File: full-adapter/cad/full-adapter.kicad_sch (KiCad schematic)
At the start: 0 parts

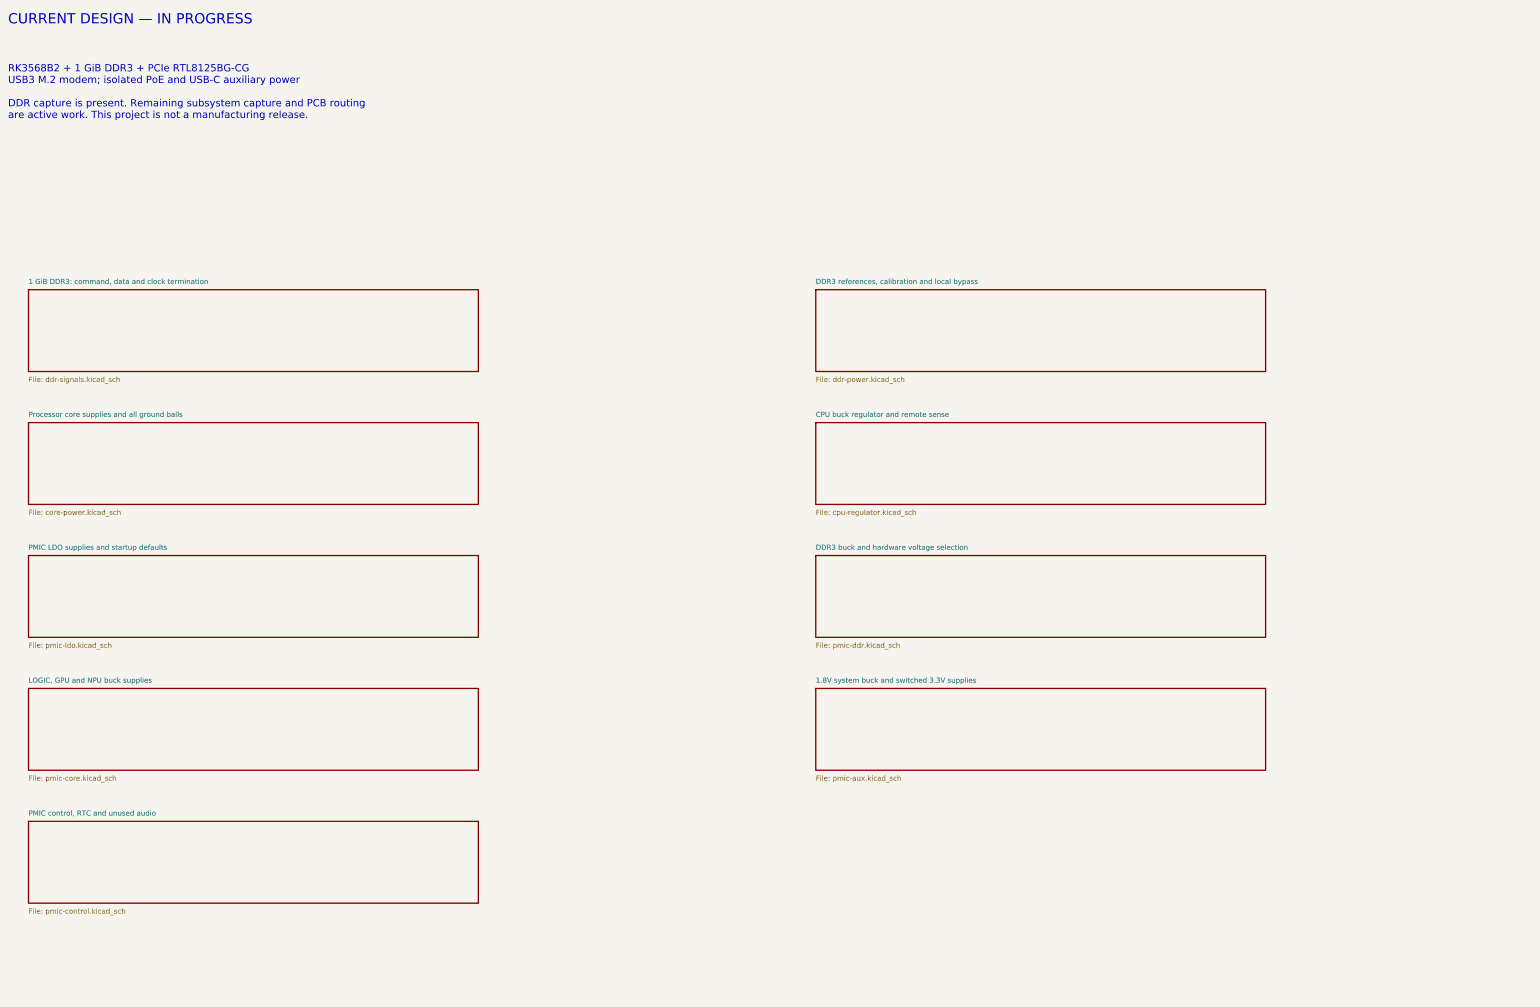
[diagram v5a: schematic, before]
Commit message: Capture processor analog and IO supplies with USB filtering
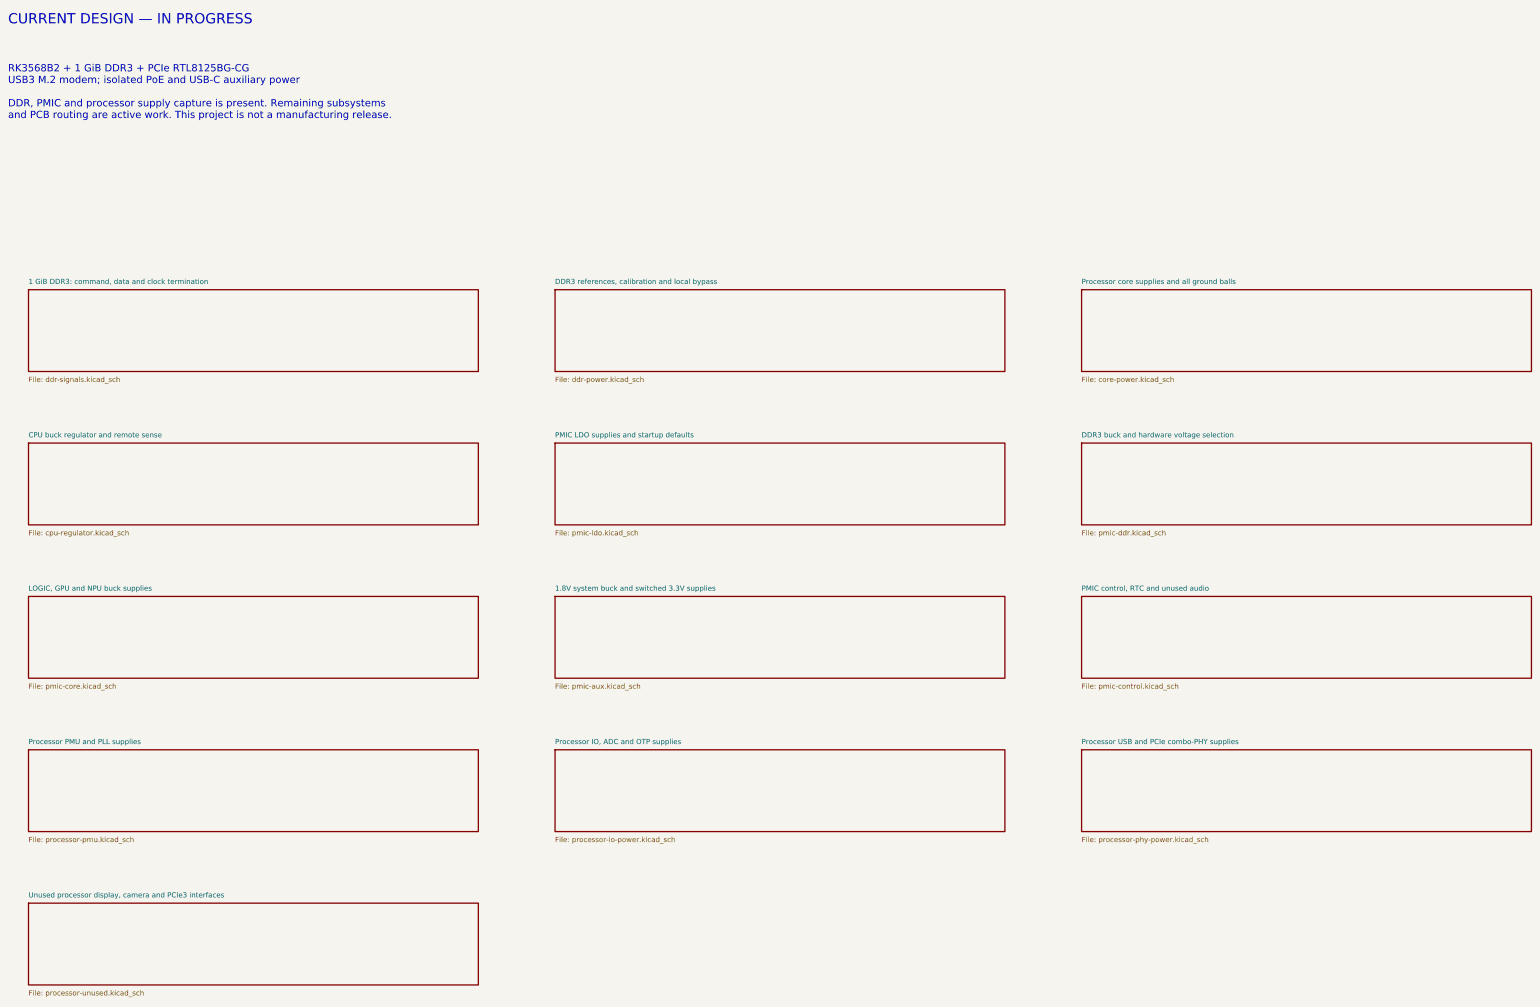
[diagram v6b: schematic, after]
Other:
- added sheet Processor IO, ADC and OTP supplies (processor-io-power.kicad_sch)
- added sheet Processor PMU and PLL supplies (processor-pmu.kicad_sch)
- added sheet Processor USB and PCIe combo-PHY supplies (processor-phy-power.kicad_sch)
- added sheet Unused processor display, camera and PCIe3 interfaces (processor-unused.kicad_sch)
- note added: "RK3568B2 + 1 GiB DDR3 + PCIe RTL8125BG-CG USB3 M.2 modem; isolated PoE and USB-C auxiliary power DDR, PMIC and processor supply capture is present. Remaining subsystems and PCB routing are active work. This project is not a manufacturing release."
- note removed: "RK3568B2 + 1 GiB DDR3 + PCIe RTL8125BG-CG USB3 M.2 modem; isolated PoE and USB-C auxiliary power DDR capture is present. Remaining subsystem capture and PCB routing are active work. This project is not a manufacturing release."
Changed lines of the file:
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@@
 (title_block (title "Integrated Linux USB3 modem / 2.5GbE development board") (rev "WORK IN PROGRESS") (company "Integrated modem development board"))
 (text "CURRENT DESIGN — IN PROGRESS" (at 20.32 20.32 0) (effects (font (size 2.54 2.54)) (justify left top)))
-(text "RK3568B2 + 1 GiB DDR3 + PCIe RTL8125BG-CG\nUSB3 M.2 modem; isolated PoE and USB-C auxiliary power\n\nDDR capture is present. Remaining subsystem capture and PCB routing\nare active work. This project is not a manufacturing release." (at 20.32 33.02 0) (effects (font (size 1.8 1.8)) (justify left top)))
+(text "RK3568B2 + 1 GiB DDR3 + PCIe RTL8125BG-CG\nUSB3 M.2 modem; isolated PoE and USB-C auxiliary power\n\nDDR, PMIC and processor supply capture is present. Remaining subsystems\nand PCB routing are active work. This project is not a manufacturing release." (at 20.32 33.02 0) (effects (font (size 1.8 1.8)) (justify left top)))
 (sheet (at 25.4 88.9) (size 111.76 20.32) (fields_autoplaced yes) (stroke (width 0.254) (type default)) (fill (color 0 0 0 0)) (property "Sheetname" "1 GiB DDR3: command, data and clock termination" (at 25.4 87.63000000000001 0) (effects (font (size 1.27 1.27)) (justify left bottom))) (property "Sheetfile" "ddr-signals.kicad_sch" (at 25.4 110.49000000000001 0) (effects (font (size 1.27 1.27)) (justify left top))))
-(sheet (at 220.98000000000002 88.9) (size 111.76 20.32) (fields_autoplaced yes) (stroke (width 0.254) (type default)) (fill (color 0 0 0 0)) (property "Sheetname" "DDR3 references, calibration and local bypass" (at 220.98000000000002 87.63000000000001 0) (effects (font (size 1.27 1.27)) (justify left bottom))) (property "Sheetfile" "ddr-power.kicad_sch" (at 220.98000000000002 110.49000000000001 0) (effects (font (size 1.27 1.27)) (justify left top))))
-(sheet (at 25.4 121.92000000000002) (size 111.76 20.32) (fields_autoplaced yes) (stroke (width 0.254) (type default)) (fill (color 0 0 0 0)) (property "Sheetname" "Processor core supplies and all ground balls" (at 25.4 120.65000000000002 0) (effects (font (size 1.27 1.27)) (justify left bottom))) (property "Sheetfile" "core-power.kicad_sch" (at 25.4 143.51000000000002 0) (effects (font (size 1.27 1.27)) (justify left top))))
-(sheet (at 220.98000000000002 121.92000000000002) (size 111.76 20.32) (fields_autoplaced yes) (stroke (width 0.254) (type default)) (fill (color 0 0 0 0)) (property "Sheetname" "CPU buck regulator and remote sense" (at 220.98000000000002 120.65000000000002 0) (effects (font (size 1.27 1.27)) (justify left bottom))) (property "Sheetfile" "cpu-regulator.kicad_sch" (at 220.98000000000002 143.51000000000002 0) (effects (font (size 1.27 1.27)) (justify left top))))
-(sheet (at 25.4 154.94) (size 111.76 20.32) (fields_autoplaced yes) (stroke (width 0.254) (type default)) (fill (color 0 0 0 0)) (property "Sheetname" "PMIC LDO supplies and startup defaults" (at 25.4 153.67 0) (effects (font (size 1.27 1.27)) (justify left bottom))) (property "Sheetfile" "pmic-ldo.kicad_sch" (at 25.4 176.53 0) (effects (font (size 1.27 1.27)) (justify left top))))
-(sheet (at 220.98000000000002 154.94) (size 111.76 20.32) (fields_autoplaced yes) (stroke (width 0.254) (type default)) (fill (color 0 0 0 0)) (property "Sheetname" "DDR3 buck and hardware voltage selection" (at 220.98000000000002 153.67 0) (effects (font (size 1.27 1.27)) (justify left bottom))) (property "Sheetfile" "pmic-ddr.kicad_sch" (at 220.98000000000002 176.53 0) (effects (font (size 1.27 1.27)) (justify left top))))
-(sheet (at 25.4 187.96) (size 111.76 20.32) (fields_autoplaced yes) (stroke (width 0.254) (type default)) (fill (color 0 0 0 0)) (property "Sheetname" "LOGIC, GPU and NPU buck supplies" (at 25.4 186.69 0) (effects (font (size 1.27 1.27)) (justify left bottom))) (property "Sheetfile" "pmic-core.kicad_sch" (at 25.4 209.55 0) (effects (font (size 1.27 1.27)) (justify left top))))
-(sheet (at 220.98000000000002 187.96) (size 111.76 20.32) (fields_autoplaced yes) (stroke (width 0.254) (type default)) (fill (color 0 0 0 0)) (property "Sheetname" "1.8V system buck and switched 3.3V supplies" (at 220.98000000000002 186.69 0) (effects (font (size 1.27 1.27)) (justify left bottom))) (property "Sheetfile" "pmic-aux.kicad_sch" (at 220.98000000000002 209.55 0) (effects (font (size 1.27 1.27)) (justify left top))))
-(sheet (at 25.4 220.98000000000002) (size 111.76 20.32) (fields_autoplaced yes) (stroke (width 0.254) (type default)) (fill (color 0 0 0 0)) (property "Sheetname" "PMIC control, RTC and unused audio" (at 25.4 219.71 0) (effects (font (size 1.27 1.27)) (justify left bottom))) (property "Sheetfile" "pmic-control.kicad_sch" (at 25.4 242.57000000000002 0) (effects (font (size 1.27 1.27)) (justify left top))))
+(sheet (at 156.21 88.9) (size 111.76 20.32) (fields_autoplaced yes) (stroke (width 0.254) (type default)) (fill (color 0 0 0 0)) (property "Sheetname" "DDR3 references, calibration and local bypass" (at 156.21 87.63000000000001 0) (effects (font (size 1.27 1.27)) (justify left bottom))) (property "Sheetfile" "ddr-power.kicad_sch" (at 156.21 110.49000000000001 0) (effects (font (size 1.27 1.27)) (justify left top))))
+(sheet (at 287.02 88.9) (size 111.76 20.32) (fields_autoplaced yes) (stroke (width 0.254) (type default)) (fill (color 0 0 0 0)) (property "Sheetname" "Processor core supplies and all ground balls" (at 287.02 87.63000000000001 0) (effects (font (size 1.27 1.27)) (justify left bottom))) (property "Sheetfile" "core-power.kicad_sch" (at 287.02 110.49000000000001 0) (effects (font (size 1.27 1.27)) (justify left top))))
+(sheet (at 25.4 127.0) (size 111.76 20.32) (fields_autoplaced yes) (stroke (width 0.254) (type default)) (fill (color 0 0 0 0)) (property "Sheetname" "CPU buck regulator and remote sense" (at 25.4 125.73 0) (effects (font (size 1.27 1.27)) (justify left bottom))) (property "Sheetfile" "cpu-regulator.kicad_sch" (at 25.4 148.59 0) (effects (font (size 1.27 1.27)) (justify left top))))
+(sheet (at 156.21 127.0) (size 111.76 20.32) (fields_autoplaced yes) (stroke (width 0.254) (type default)) (fill (color 0 0 0 0)) (property "Sheetname" "PMIC LDO supplies and startup defaults" (at 156.21 125.73 0) (effects (font (size 1.27 1.27)) (justify left bottom))) (property "Sheetfile" "pmic-ldo.kicad_sch" (at 156.21 148.59 0) (effects (font (size 1.27 1.27)) (justify left top))))
+(sheet (at 287.02 127.0) (size 111.76 20.32) (fields_autoplaced yes) (stroke (width 0.254) (type default)) (fill (color 0 0 0 0)) (property "Sheetname" "DDR3 buck and hardware voltage selection" (at 287.02 125.73 0) (effects (font (size 1.27 1.27)) (justify left bottom))) (property "Sheetfile" "pmic-ddr.kicad_sch" (at 287.02 148.59 0) (effects (font (size 1.27 1.27)) (justify left top))))
+(sheet (at 25.4 165.10000000000002) (size 111.76 20.32) (fields_autoplaced yes) (stroke (width 0.254) (type default)) (fill (color 0 0 0 0)) (property "Sheetname" "LOGIC, GPU and NPU buck supplies" (at 25.4 163.83 0) (effects (font (size 1.27 1.27)) (justify left bottom))) (property "Sheetfile" "pmic-core.kicad_sch" (at 25.4 186.69000000000003 0) (effects (font (size 1.27 1.27)) (justify left top))))
+(sheet (at 156.21 165.10000000000002) (size 111.76 20.32) (fields_autoplaced yes) (stroke (width 0.254) (type default)) (fill (color 0 0 0 0)) (property "Sheetname" "1.8V system buck and switched 3.3V supplies" (at 156.21 163.83 0) (effects (font (size 1.27 1.27)) (justify left bottom))) (property "Sheetfile" "pmic-aux.kicad_sch" (at 156.21 186.69000000000003 0) (effects (font (size 1.27 1.27)) (justify left top))))
+(sheet (at 287.02 165.10000000000002) (size 111.76 20.32) (fields_autoplaced yes) (stroke (width 0.254) (type default)) (fill (color 0 0 0 0)) (property "Sheetname" "PMIC control, RTC and unused audio" (at 287.02 163.83 0) (effects (font (size 1.27 1.27)) (justify left bottom))) (property "Sheetfile" "pmic-control.kicad_sch" (at 287.02 186.69000000000003 0) (effects (font (size 1.27 1.27)) (justify left top))))
+(sheet (at 25.4 203.20000000000002) (size 111.76 20.32) (fields_autoplaced yes) (stroke (width 0.254) (type default)) (fill (color 0 0 0 0)) (property "Sheetname" "Processor PMU and PLL supplies" (at 25.4 201.93 0) (effects (font (size 1.27 1.27)) (justify left bottom))) (property "Sheetfile" "processor-pmu.kicad_sch" (at 25.4 224.79000000000002 0) (effects (font (size 1.27 1.27)) (justify left top))))
+(sheet (at 156.21 203.20000000000002) (size 111.76 20.32) (fields_autoplaced yes) (stroke (width 0.254) (type default)) (fill (color 0 0 0 0)) (property "Sheetname" "Processor IO, ADC and OTP supplies" (at 156.21 201.93 0) (effects (font (size 1.27 1.27)) (justify left bottom))) (property "Sheetfile" "processor-io-power.kicad_sch" (at 156.21 224.79000000000002 0) (effects (font (size 1.27 1.27)) (justify left top))))
+(sheet (at 287.02 203.20000000000002) (size 111.76 20.32) (fields_autoplaced yes) (stroke (width 0.254) (type default)) (fill (color 0 0 0 0)) (property "Sheetname" "Processor USB and PCIe combo-PHY supplies" (at 287.02 201.93 0) (effects (font (size 1.27 1.27)) (justify left bottom))) (property "Sheetfile" "processor-phy-power.kicad_sch" (at 287.02 224.79000000000002 0) (effects (font (size 1.27 1.27)) (justify left top))))
+(sheet (at 25.4 241.3) (size 111.76 20.32) (fields_autoplaced yes) (stroke (width 0.254) (type default)) (fill (color 0 0 0 0)) (property "Sheetname" "Unused processor display, camera and PCIe3 interfaces" (at 25.4 240.03 0) (effects (font (size 1.27 1.27)) (justify left bottom))) (property "Sheetfile" "processor-unused.kicad_sch" (at 25.4 262.89 0) (effects (font (size 1.27 1.27)) (justify left top))))
 )

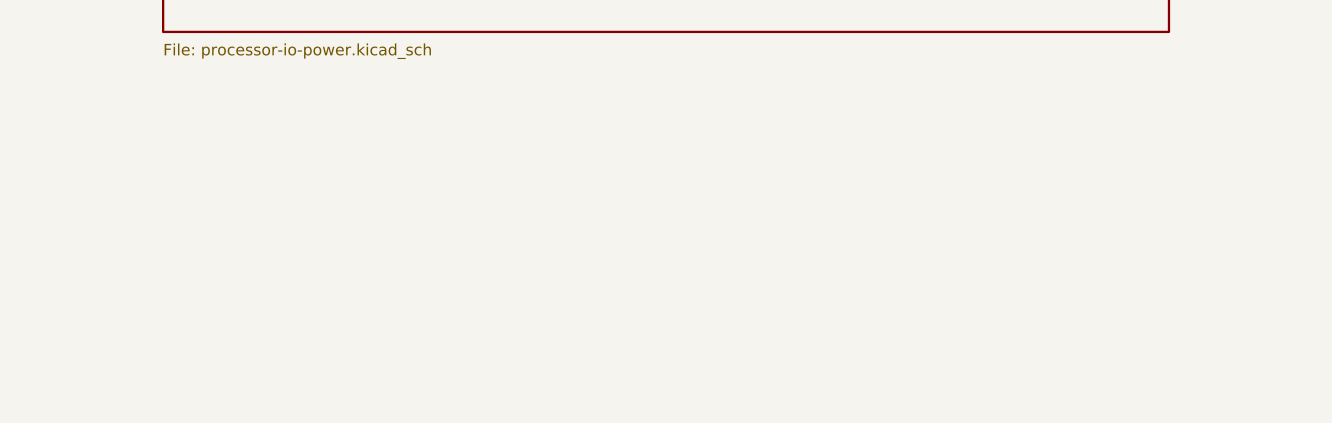
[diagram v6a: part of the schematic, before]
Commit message: Connect processor PMIC controls and hardware boot straps
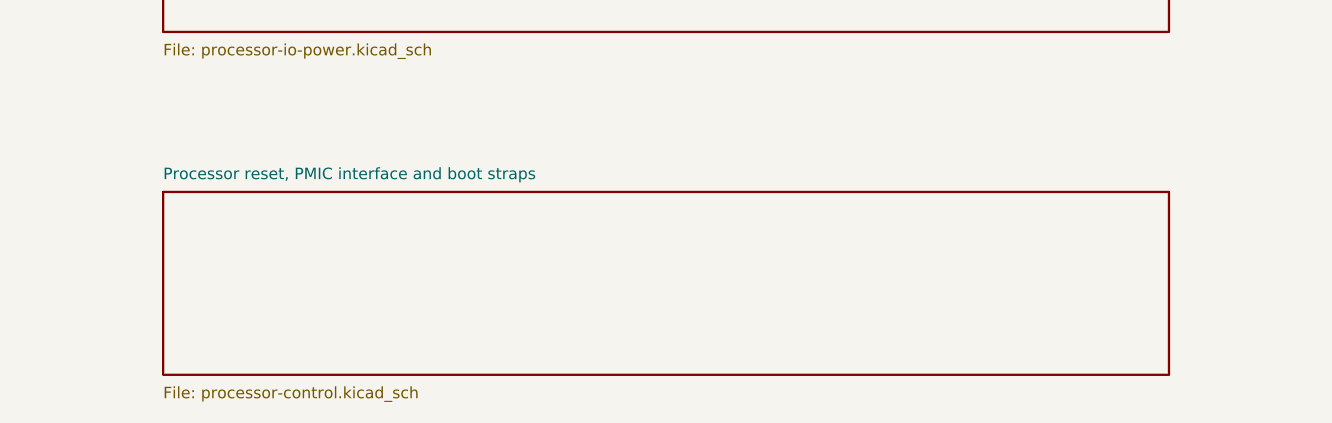
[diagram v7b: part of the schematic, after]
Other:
- added sheet Processor reset, PMIC interface and boot straps (processor-control.kicad_sch)
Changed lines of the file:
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@@
 (sheet (at 287.02 203.20000000000002) (size 111.76 20.32) (fields_autoplaced yes) (stroke (width 0.254) (type default)) (fill (color 0 0 0 0)) (property "Sheetname" "Processor USB and PCIe combo-PHY supplies" (at 287.02 201.93 0) (effects (font (size 1.27 1.27)) (justify left bottom))) (property "Sheetfile" "processor-phy-power.kicad_sch" (at 287.02 224.79000000000002 0) (effects (font (size 1.27 1.27)) (justify left top))))
 (sheet (at 25.4 241.3) (size 111.76 20.32) (fields_autoplaced yes) (stroke (width 0.254) (type default)) (fill (color 0 0 0 0)) (property "Sheetname" "Unused processor display, camera and PCIe3 interfaces" (at 25.4 240.03 0) (effects (font (size 1.27 1.27)) (justify left bottom))) (property "Sheetfile" "processor-unused.kicad_sch" (at 25.4 262.89 0) (effects (font (size 1.27 1.27)) (justify left top))))
+(sheet (at 156.21 241.3) (size 111.76 20.32) (fields_autoplaced yes) (stroke (width 0.254) (type default)) (fill (color 0 0 0 0)) (property "Sheetname" "Processor reset, PMIC interface and boot straps" (at 156.21 240.03 0) (effects (font (size 1.27 1.27)) (justify left bottom))) (property "Sheetfile" "processor-control.kicad_sch" (at 156.21 262.89 0) (effects (font (size 1.27 1.27)) (justify left top))))
 )
